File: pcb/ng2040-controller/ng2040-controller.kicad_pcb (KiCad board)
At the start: 2 copper layers, 0 parts

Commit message: controller board
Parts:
- added C1: 1uF, Capacitor_SMD:C_0805_2012Metric_Pad1.18x1.45mm_HandSolder, B.Cu at (56.0, 61.5)
- added H1: MountingHole_2.7mm_M2.5, MountingHole:MountingHole_2.7mm_M2.5, F.Cu at (102.0, 71.0)
- added H2: MountingHole_2.7mm_M2.5, MountingHole:MountingHole_2.7mm_M2.5, F.Cu at (41.5, 71.0)
- added H3: MountingHole_2.7mm_M2.5, MountingHole:MountingHole_2.7mm_M2.5, F.Cu at (102.0, 43.0)
- added H4: MountingHole_2.7mm_M2.5, MountingHole:MountingHole_2.7mm_M2.5, F.Cu at (41.5, 43.0)
- added J1: A, Connector_JST:JST_XH_B2B-XH-A_1x02_P2.50mm_Vertical, F.Cu at (75.6, 69.0)
- added J2: B, Connector_JST:JST_XH_B2B-XH-A_1x02_P2.50mm_Vertical, F.Cu at (66.6, 69.0)
- added J3: C, Connector_JST:JST_XH_B2B-XH-A_1x02_P2.50mm_Vertical, F.Cu at (57.9, 69.0)
- added J4: D, Connector_JST:JST_XH_B2B-XH-A_1x02_P2.50mm_Vertical, F.Cu at (49.1, 69.0)
- added J5: START, Connector_JST:JST_XH_B2B-XH-A_1x02_P2.50mm_Vertical, F.Cu at (70.8, 60.0)
- added J6: SELECT, Connector_JST:JST_XH_B2B-XH-A_1x02_P2.50mm_Vertical, F.Cu at (61.8, 60.0)
- added J7: JOY, Connector_JST:JST_XH_B5B-XH-A_1x05_P2.50mm_Vertical, F.Cu at (85.0, 69.0)
- added J8: BATTERY, Connector_JST:JST_PH_B2B-PH-K_1x02_P2.00mm_Vertical, F.Cu at (40.5, 58.0)
- added SW1: OPTS, Button_Switch_THT:SW_DIP_SPSTx02_Slide_9.78x7.26mm_W7.62mm_P2.54mm, F.Cu at (64.2, 42.7)
- added U1: RP2040-Zero, RP2040Zero:RP2040-Zero, F.Cu at (77.3, 64.1)
- added U2: NRF24L01_Breakout, NRF24L01:NRF24L01-SMD, B.Cu at (51.5, 49.5)
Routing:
- added copper zone on B.Cu, net GND
- added copper zone on F.Cu, net GND
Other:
- board outline added: 67.5 x 35 mm

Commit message: NG2040 controller board
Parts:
- U2: value NRF24L01_Breakout -> NRF24L01
- moved C1 6.71 mm to (59.0, 55.5), turned to 90 degrees
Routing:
- net /VBATT: track 0.00 -> 48.7 mm
- net /MOSI: track 0.00 -> 45.4 mm
- net /BD: track 0.00 -> 44.3 mm
- net /MISO: track 0.00 -> 43.2 mm
- net /BC: track 0.00 -> 38.1 mm
- net /BB: track 0.00 -> 36.9 mm
- net /IRQ: track 0.00 -> 35.9 mm
- net /CS: track 0.00 -> 35.8 mm
- net /CE: track 0.00 -> 33.7 mm
- net /SCK: track 0.00 -> 33.7 mm
- net /BA: track 0.00 -> 31.2 mm
- net /DL: track 0.00 -> 30.8 mm
- net /DR: track 0.00 -> 29.2 mm
- net /3V3: track 0.00 -> 28.8 mm, vias 0 -> 1
- net /DU: track 0.00 -> 28.5 mm
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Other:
- outline, holes or cut-outs redrawn
- board text added: "${TITLE} rev.${REVISION} ${COMPANY}"
- board text added: "+"
- board text added: "-"
- board text added: "HIGH"
- board text added: "JLCJLCJLCJLC"
- board text added: "LOW"
- board text added: "P1"
- board text added: "P2"
- board text added: "PLAYER"
- board text added: "POWER"

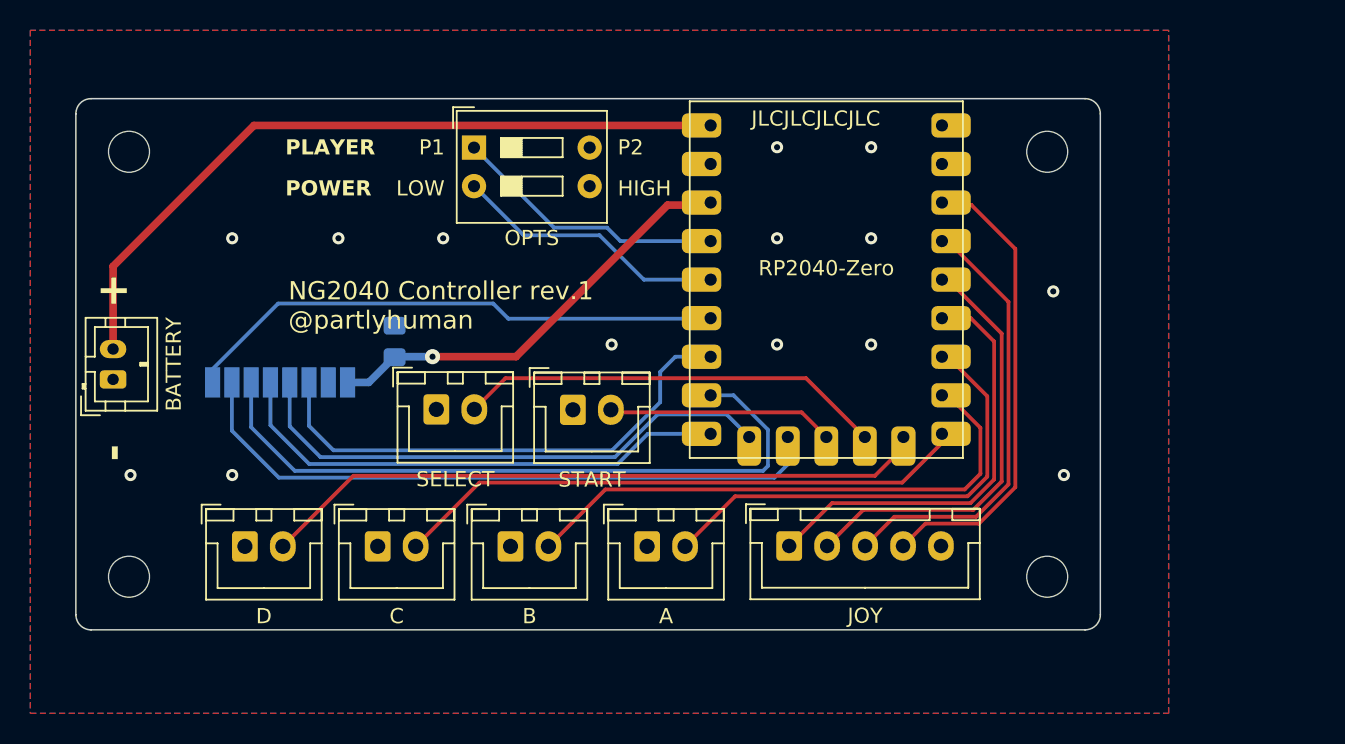
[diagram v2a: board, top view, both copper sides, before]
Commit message: Reworking controller board to put pico on back for LED to shine through
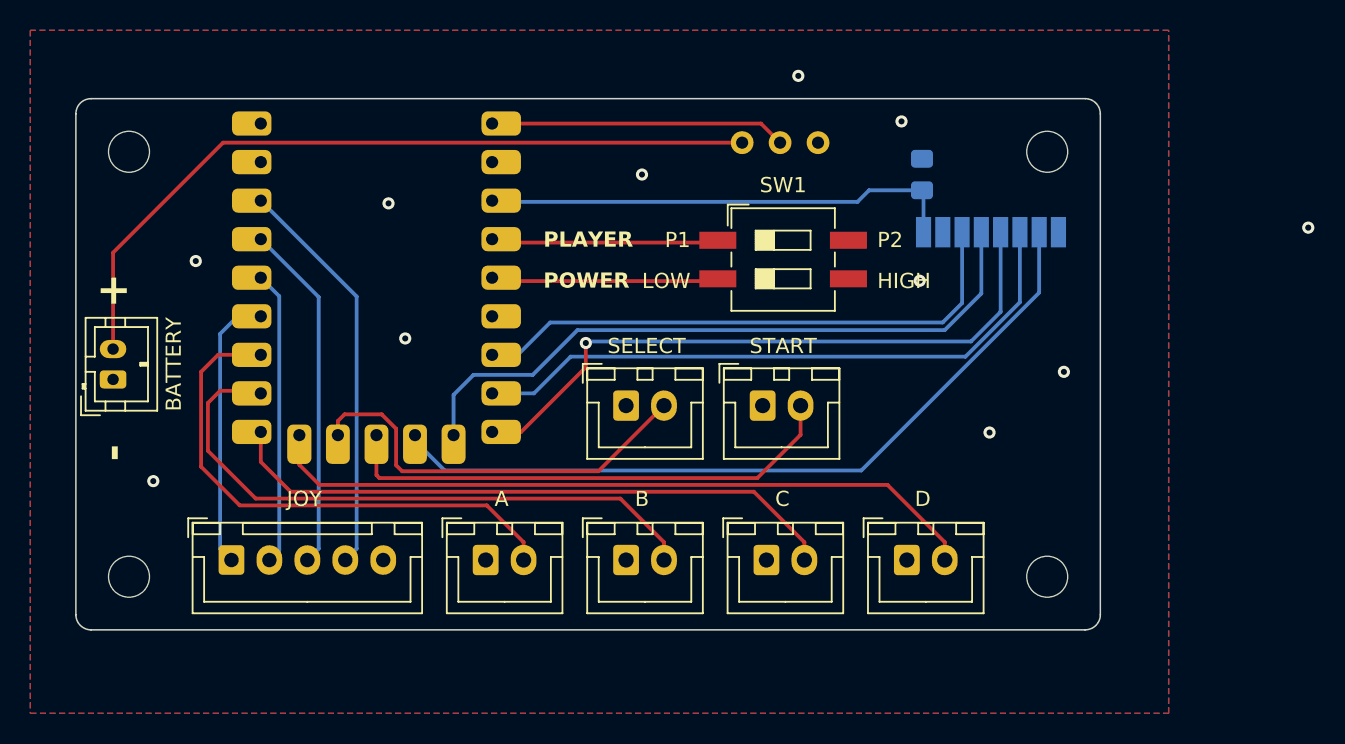
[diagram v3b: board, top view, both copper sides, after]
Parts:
- added SW2: POWER, REB_Switch:REB_SlideSwitch_3pin, B.Cu at (86.9, 42.4)
- SW1: footprint Button_Switch_THT:SW_DIP_SPSTx02_Slide_9.78x7.26mm_W7.62mm_P2.54mm -> Button_Switch_SMD:SW_DIP_SPSTx02_Slide_6.7x6.64mm_W8.61mm_P2.54mm_LowProfile
- U1: moved to B.Cu
- moved U2 47.3 mm to (98.2, 57.0), turned to 0 degrees
- moved J4 43.6 mm to (92.8, 69.9)
- moved J7 36.8 mm to (48.2, 69.9)
- moved C1 36.4 mm to (93.8, 44.5)
- moved J3 25.6 mm to (83.5, 69.9)
- moved SW1 21.7 mm to (84.6, 50.1)
- moved J5 12.5 mm to (83.2, 59.7)
- moved J6 12.5 mm to (74.2, 59.7)
- moved J1 10.7 mm to (65.0, 69.9)
- moved U1 9.32 mm to (68.0, 64.0), turned to 180 degrees
- moved J2 7.67 mm to (74.2, 69.9)
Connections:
- J8 pad 2: /VBATT -> Net-(J8-Pin_2)
- U1 pad 18: /IRQ -> unconnected-(U1-GP27-Pad18)
- U2 pad 8: /IRQ -> unconnected-(U2-IRQ-Pad8)
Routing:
- net Net-(J8-Pin_2): track 0.00 -> 50.8 mm
- net /IRQ: track 35.9 -> 0.00 mm
- net /VBATT: track 48.7 -> 19.5 mm
- net /STA: track 14.9 -> 33.8 mm
- net /DU: track 28.5 -> 18.5 mm
- net /SCK: track 33.7 -> 43.0 mm, vias 0 -> 1
- net /DD: track 28.4 -> 19.4 mm
- net /CS: track 35.8 -> 44.2 mm
- net /MISO: track 43.2 -> 51.1 mm
- net /DR: track 29.2 -> 23.0 mm
- net /DL: track 30.8 -> 26.6 mm
- net /BA: track 31.2 -> 35.1 mm
- net /BB: track 36.9 -> 40.8 mm
- net /MOSI: track 45.4 -> 41.9 mm
- net /BD: track 44.3 -> 47.8 mm
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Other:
- board text added: "OFF"
- board text added: "ON"
- board text removed: "${TITLE} rev.${REVISION} ${COMPANY}"
